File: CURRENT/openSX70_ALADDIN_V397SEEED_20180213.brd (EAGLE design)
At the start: 95.9 x 27.9 mm, 45 parts, among them Q1 2N7002, Q2 2N7002, Q3 MMBT3904LT1G, U1 ATMEGA328P_TQFP, U3 BH1750FVI-TR, Y1 CSTCE8M00G52Z-R0

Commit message: New BOM and new PCB all OPL CPL parts for manufacturing!
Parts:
- added R15: CRCW0603100RFKEA, Common-Parts-Library-Eagle:CRCW0603100RFKEA_RESC1608X55
- D1, D2, D3: device zetex:SOD323 -> Common-Parts-Library-Eagle:SODFL2512X100N
- R2, R4: device resistor:R0603 -> Common-Parts-Library-Eagle:ERJ-3EKF1003V_RESC1608X55
- moved R2 1.40 mm to (80.8, 8.95)
- moved D1 0.51 mm to (81.9, 7.24)
- moved R1 0.45 mm to (77.6, 9.59)
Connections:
- new net N$28: Q3.2, R15.2
- net 3.3V: now also D3.C; no longer D3.1
- net 6V: now also D1.C, D2.C; no longer D1.1, D2.1
- net BUZZER-: now also D3.A; no longer D3.2
- net GND: now also R15.1; no longer Q3.2
- net SOL1-: now also D1.A; no longer D1.2
- net SOL2-: now also D2.A; no longer D2.2
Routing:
- net N$28: track 0.00 -> 2.20 mm
- net GND: track 30.6 -> 28.8 mm
- net BUZZER: track 88.9 -> 87.2 mm
- net N$1: track 7.13 -> 8.11 mm
- net SOL1-: track 10.0 -> 9.27 mm
- net BUZZER-: track 19.2 -> 18.5 mm
- net 6V: track 181.9 -> 181.2 mm
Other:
- board text added: "20180213"
- board text added: "BUZZ-AMP."
- board text removed: "2018013"
- board text removed: "BUZZER-AMPL."

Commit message: Cleaned the schematic a bit
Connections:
- net RXD renamed 100R
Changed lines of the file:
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@@
 <via x="66.548" y="20.193" extent="1-16" drill="0.35"/>
 </signal>
-<signal name="RXD">
+<signal name="100R">
 <contactref element="U1" pad="30"/>
 <wire x1="79.41945" y1="15.83055" x2="77.37475" y2="17.8435" width="0.2032" layer="1"/>

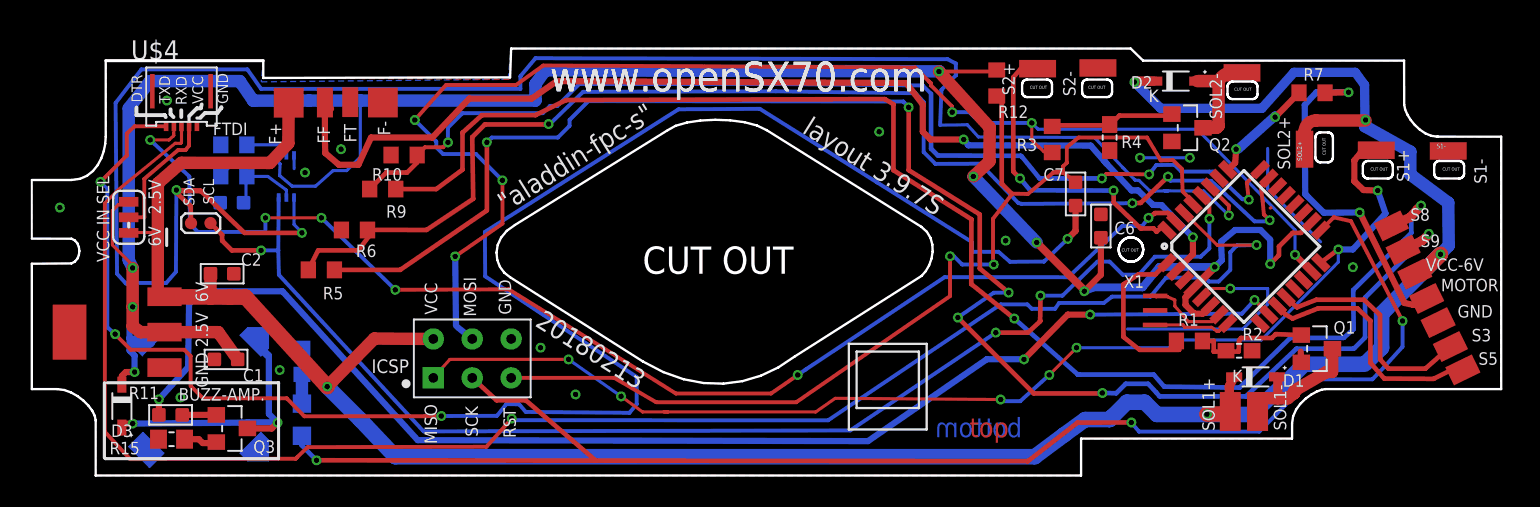
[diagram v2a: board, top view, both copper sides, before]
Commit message: changes, octopart BOM
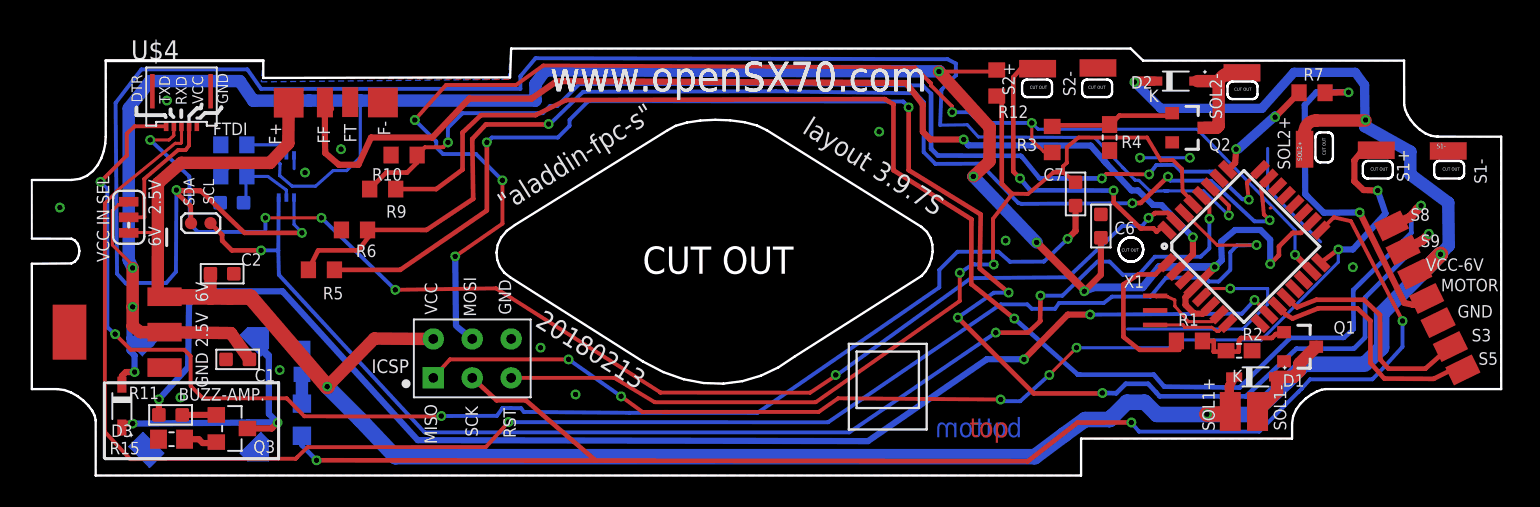
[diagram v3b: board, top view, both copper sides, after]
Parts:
- Q1, Q2: value 2N7002 -> 5.8A/30V/35mΩ; device Seeed-Transistor:SOT-23 -> openSX70:SOT23-3
- moved Q1 1.15 mm to (84.8, 9.21)
- moved C1 0.76 mm to (15.5, 8.38)
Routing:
- net DTR: track 118.5 -> 90.3 mm
- net SOL1-: track 9.27 -> 6.45 mm
- net N$1: track 8.11 -> 7.00 mm
- net GND: track 28.8 -> 27.9 mm
- net RST: track 67.9 -> 67.0 mm
- net 3.3V: track 159.5 -> 160.3 mm
